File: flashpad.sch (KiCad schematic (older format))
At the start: 23 parts, among them SW1 BOOT, SW2 RESET, U1 ATmega328P-PU, U2 ATmega32A-PU

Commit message: rev2
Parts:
- removed C3, C4, C5: 100n, Capacitor_THT:C_Disc_D5.0mm_W2.5mm_P2.50mm, symbol Device:C_Small
- removed ISP1: AVR-ISP-6, Connector_PinHeader_2.54mm:PinHeader_2x03_P2.54mm_Horizontal, symbol Connector:AVR-ISP-6
- removed R5: 1.5K, Resistor_THT:R_Axial_DIN0204_L3.6mm_D1.6mm_P7.62mm_Horizontal, symbol Device:R
- removed SW1: BOOT, Button_Switch_THT:SW_PUSH_6mm, symbol Switch:SW_Push
- removed SW2: RESET, Button_Switch_THT:SW_PUSH_6mm, symbol Switch:SW_Push
- removed USB1: USB_B_Mini, custom_parts:USB_Mini, symbol Connector:USB_B_Mini
- added C1: 22p, Capacitor_THT:C_Disc_D5.0mm_W2.5mm_P5.00mm, symbol Device:C_Small
- added C8, C9: 100n, Capacitor_THT:C_Disc_D5.0mm_W2.5mm_P2.50mm, symbol Device:C_Small
- added J1: AVR-ISP-10, Connector_PinHeader_2.54mm:PinHeader_2x05_P2.54mm_Vertical, symbol Connector:AVR-ISP-10
- added JP1: SelfProg, Connector_PinHeader_2.54mm:PinHeader_1x02_P2.54mm_Vertical, symbol Device:Jumper
- added JP2: SlowSCK, Connector_PinHeader_2.54mm:PinHeader_1x02_P2.54mm_Vertical, symbol Device:Jumper
- added LED2: LED, LED_THT:LED_D5.0mm, symbol Device:LED
- added R1: 10k, Resistor_THT:R_Axial_DIN0204_L3.6mm_D1.6mm_P7.62mm_Horizontal, symbol Device:R
- added R10, R9: 1.5K, Resistor_THT:R_Axial_DIN0204_L3.6mm_D1.6mm_P7.62mm_Horizontal, symbol Device:R
- added R2, R3: 270r, Resistor_THT:R_Axial_DIN0204_L3.6mm_D1.6mm_P7.62mm_Horizontal, symbol Device:R
- added U1: ATmega8A-PU, Package_DIP:DIP-28_W7.62mm, symbol MCU_Microchip_ATmega:ATmega8A-PU
- added USB1: USB_B, Connector_USB:USB_B_OST_USB-B1HSxx_Horizontal, symbol Connector:USB_B
- added X1: 12Mhz, Crystal:Crystal_HC49-4H_Vertical, symbol Device:Crystal
- C2: value 100n -> 22p; footprint Capacitor_THT:C_Disc_D5.0mm_W2.5mm_P2.50mm -> Capacitor_THT:C_Disc_D5.0mm_W2.5mm_P5.00mm
- LED1: footprint LED_THT:LED_D3.0mm -> LED_THT:LED_D5.0mm
- R4: value 1.5K -> 270r
- R5: renamed from R1; value 1.5K -> 2.2k
- U2: footprint Package_DIP:DIP-40_W15.24mm_Socket -> Socket:DIP_Socket-40_W11.9_W12.7_W15.24_W17.78_W18.5_3M_240-1280-00-0602J
- U3: renamed from U1; footprint Package_DIP:DIP-28_W7.62mm_Socket -> custom_parts:DIP_Socket-28_flipped
- X2: renamed from XTAL1; value Crystal -> 16Mhz
- renumbered C6 to C10, C7 to C11, C1 to C3, R2 to R6, R3 to R7
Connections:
- net +5V: now also C8.1, C9.1, J1.2 (VCC), R1.1, U1.20 (AVCC), U1.7 (VCC); no longer C2.1, LED1.2 (A), R4.2
- net D+: now also U1.15 (PB1), U1.4 (PD2); no longer U2.16 (PD2), U3.4 (PD2)
- net D-: now also U1.14 (PB0); no longer U2.17 (PD3), U3.5 (PD3)
- net GND: now also C1.2, C8.2, C9.2, J1.10 (GND), J1.4 (GND), J1.6 (GND), J1.8 (GND), JP2.2, R10.1, R9.1, U1.22 (AGND), U1.8 (GND), USB1.4 (GND), USB1.5 (Shield)
- net MISO: now also U2.7 (PB6), J1.9 (MISO), U1.18 (PB4); no longer U2.6 (PB5)
- net MOSI: now also U2.6 (PB5), J1.1 (MOSI), R3.2; no longer U2.5 (PB4)
- net RESET: now also J1.5 (~RST), JP1.2, R1.2, U1.1 (PC6/~RESET); no longer R4.1
- net SCK: now also R4.2, U2.8 (PB7), J1.7 (SCK); no longer U2.7 (PB6)
- net VCC: now also USB1.1 (VBUS)
- net at D1.1 (K), R5.2, R7.1: now also USB1.2 (D-)
- net at D2.1 (K), R6.1: now also USB1.3 (D+)
- net at LED1.1 (K): now also R9.2
- net BOOT: no longer names the net of U3.6 (PD4)
- net BOOT: no longer U2.18 (PD4)
- net XTAL1 renamed XTAL2_1
- net XTAL2 renamed XTAL2_2
- new net: JP2.1, U1.25 (PC2)
- new net: JP1.1, R2.2
- new net: R2.1, U1.16 (PB2)
- new net: R3.1, U1.17 (PB3)
- new net: R4.1, U1.19 (PB5)
- new net: LED2.1 (K), R10.2
- new net LED1: LED1.2 (A), U1.23 (PC0)
- new net LED2: LED2.2 (A), U1.24 (PC1)
- new net XTAL1_1: C1.1, U1.9 (PB6/XTAL1), X1.1
- new net XTAL1_2: C2.1, U1.10 (PB7/XTAL2), X1.2
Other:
- moved on the sheet: C10, C11, C3, D1, D2, F1, R5, R6, R7, U2, U3, X2

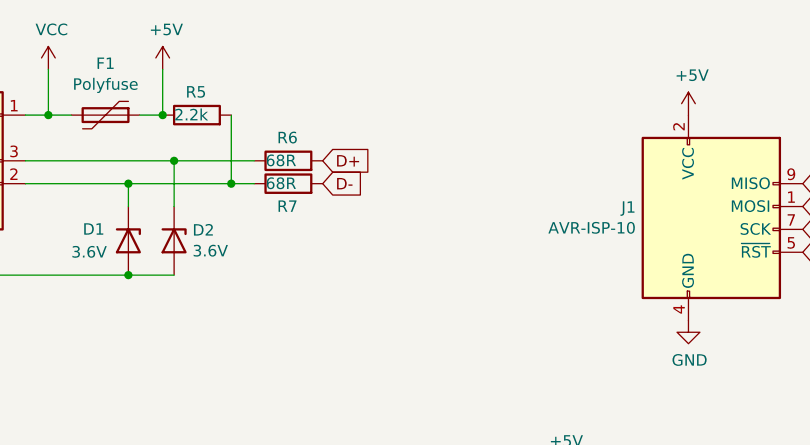
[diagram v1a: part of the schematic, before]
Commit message: fix footprints
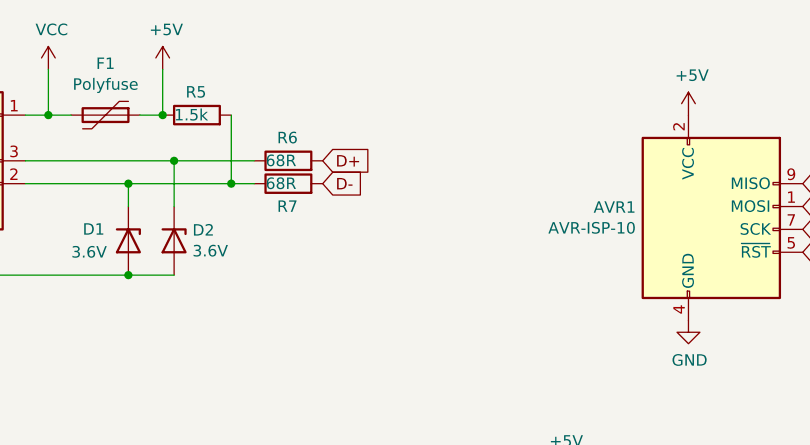
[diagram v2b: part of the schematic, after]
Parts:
- removed J1: AVR-ISP-10, Connector_PinHeader_2.54mm:PinHeader_2x05_P2.54mm_Vertical, symbol Connector:AVR-ISP-10
- added AVR1: AVR-ISP-10, Connector_IDC:IDC-Header_2x05_P2.54mm_Vertical, symbol Connector:AVR-ISP-10
- R1, R10, R2, R3, R4, R6, R7, R9: footprint Resistor_THT:R_Axial_DIN0204_L3.6mm_D1.6mm_P7.62mm_Horizontal -> Resistor_THT:R_Axial_DIN0207_L6.3mm_D2.5mm_P10.16mm_Horizontal
- R5: value 2.2k -> 1.5k; footprint Resistor_THT:R_Axial_DIN0204_L3.6mm_D1.6mm_P7.62mm_Horizontal -> Resistor_THT:R_Axial_DIN0207_L6.3mm_D2.5mm_P10.16mm_Horizontal
- U2: footprint Socket:DIP_Socket-40_W11.9_W12.7_W15.24_W17.78_W18.5_3M_240-1280-00-0602J -> custom_parts:socket40dip
- U3: footprint custom_parts:DIP_Socket-28_flipped -> custom_parts:socket28dip
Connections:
- net +5V: now also AVR1.2 (VCC)
- net GND: now also AVR1.10 (GND), AVR1.4 (GND), AVR1.6 (GND), AVR1.8 (GND)
- net MISO: now also AVR1.9 (MISO)
- net MOSI: now also AVR1.1 (MOSI)
- net RESET: now also AVR1.5 (~RST)
- net SCK: now also AVR1.7 (SCK)
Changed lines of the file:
@@
 F 0 "U3" H 7356 3746 50  0000 R CNN
 F 1 "ATmega328P-PU" H 7356 3655 50  0000 R CNN
-F 2 "custom_parts:DIP_Socket-28_flipped" H 8000 3700 50  0001 C CIN
+F 2 "custom_parts:socket28dip" H 8000 3700 50  0001 C CIN
 F 3 "http://ww1.microchip.com/downloads/en/DeviceDoc/ATmega328_P%20AVR%20MCU%20with%20picoPower%20Technology%20Data%20Sheet%2040001984A.pdf" H 8000 3700 50  0001 C CNN
 	1    8000 3700
@@
 F 0 "U2" H 10300 1650 50  0000 C CNN
 F 1 "ATmega32A-PU" H 9700 1650 50  0000 C CNN
-F 2 "Socket:DIP_Socket-40_W11.9_W12.7_W15.24_W17.78_W18.5_3M_240-1280-00-0602J" H 10150 3600 50  0001 C CIN
+F 2 "custom_parts:socket40dip" H 10150 3600 50  0001 C CIN
 F 3 "http://ww1.microchip.com/downloads/en/DeviceDoc/atmel-8155-8-bit-microcontroller-avr-atmega32a_datasheet.pdf" H 10150 3600 50  0001 C CNN
 	1    10150 3600
@@
 F 0 "R6" V 2850 1450 50  0000 R CNN
 F 1 "68R" V 2750 1500 50  0000 R CNN
-F 2 "Resistor_THT:R_Axial_DIN0204_L3.6mm_D1.6mm_P7.62mm_Horizontal" V 2680 1400 50  0001 C CNN
+F 2 "Resistor_THT:R_Axial_DIN0207_L6.3mm_D2.5mm_P10.16mm_Horizontal" V 2680 1400 50  0001 C CNN
 F 3 "~" H 2750 1400 50  0001 C CNN
 	1    2750 1400
@@
 P 2350 1200
 F 0 "R5" V 2450 1250 50  0000 R CNN
-F 1 "2.2k" V 2350 1300 50  0000 R CNN
-F 2 "Resistor_THT:R_Axial_DIN0204_L3.6mm_D1.6mm_P7.62mm_Horizontal" V 2280 1200 50  0001 C CNN
+F 1 "1.5k" V 2350 1300 50  0000 R CNN
+F 2 "Resistor_THT:R_Axial_DIN0207_L6.3mm_D2.5mm_P10.16mm_Horizontal" V 2280 1200 50  0001 C CNN
 F 3 "~" H 2350 1200 50  0001 C CNN
 	1    2350 1200
@@
 F 0 "R7" V 2650 1550 50  0000 R CNN
 F 1 "68R" V 2750 1600 50  0000 R CNN
-F 2 "Resistor_THT:R_Axial_DIN0204_L3.6mm_D1.6mm_P7.62mm_Horizontal" V 2680 1500 50  0001 C CNN
+F 2 "Resistor_THT:R_Axial_DIN0207_L6.3mm_D2.5mm_P10.16mm_Horizontal" V 2680 1500 50  0001 C CNN
 F 3 "~" H 2750 1500 50  0001 C CNN
 	1    2750 1500
@@
 F 0 "R9" V 1550 3400 50  0000 R CNN
 F 1 "1.5K" V 1450 3450 50  0000 R CNN
-F 2 "Resistor_THT:R_Axial_DIN0204_L3.6mm_D1.6mm_P7.62mm_Horizontal" V 1380 3350 50  0001 C CNN
+F 2 "Resistor_THT:R_Axial_DIN0207_L6.3mm_D2.5mm_P10.16mm_Horizontal" V 1380 3350 50  0001 C CNN
 F 3 "~" H 1450 3350 50  0001 C CNN
 	1    1450 3350
@@
 F 0 "R1" V 3050 3200 50  0000 R CNN
 F 1 "10k" V 2950 3250 50  0000 R CNN
-F 2 "Resistor_THT:R_Axial_DIN0204_L3.6mm_D1.6mm_P7.62mm_Horizontal" V 2880 3150 50  0001 C CNN
+F 2 "Resistor_THT:R_Axial_DIN0207_L6.3mm_D2.5mm_P10.16mm_Horizontal" V 2880 3150 50  0001 C CNN
 F 3 "~" H 2950 3150 50  0001 C CNN
 	1    2950 3150
@@
 F 0 "R2" V 5100 3400 50  0000 R CNN
 F 1 "270r" V 5000 3450 50  0000 R CNN
-F 2 "Resistor_THT:R_Axial_DIN0204_L3.6mm_D1.6mm_P7.62mm_Horizontal" V 4930 3350 50  0001 C CNN
+F 2 "Resistor_THT:R_Axial_DIN0207_L6.3mm_D2.5mm_P10.16mm_Horizontal" V 4930 3350 50  0001 C CNN
 F 3 "~" H 5000 3350 50  0001 C CNN
 	1    5000 3350
@@
 F 0 "R3" V 4900 3500 50  0000 R CNN
 F 1 "270r" V 4800 3550 50  0000 R CNN
-F 2 "Resistor_THT:R_Axial_DIN0204_L3.6mm_D1.6mm_P7.62mm_Horizontal" V 4730 3450 50  0001 C CNN
+F 2 "Resistor_THT:R_Axial_DIN0207_L6.3mm_D2.5mm_P10.16mm_Horizontal" V 4730 3450 50  0001 C CNN
 F 3 "~" H 4800 3450 50  0001 C CNN
 	1    4800 3450
@@
 F 0 "R4" V 5100 3700 50  0000 R CNN
 F 1 "270r" V 5000 3750 50  0000 R CNN
-F 2 "Resistor_THT:R_Axial_DIN0204_L3.6mm_D1.6mm_P7.62mm_Horizontal" V 4930 3650 50  0001 C CNN
+F 2 "Resistor_THT:R_Axial_DIN0207_L6.3mm_D2.5mm_P10.16mm_Horizontal" V 4930 3650 50  0001 C CNN
 F 3 "~" H 5000 3650 50  0001 C CNN
 	1    5000 3650
@@
 F 0 "R10" V 1550 4000 50  0000 R CNN
 F 1 "1.5K" V 1450 4050 50  0000 R CNN
-F 2 "Resistor_THT:R_Axial_DIN0204_L3.6mm_D1.6mm_P7.62mm_Horizontal" V 1380 3950 50  0001 C CNN
+F 2 "Resistor_THT:R_Axial_DIN0207_L6.3mm_D2.5mm_P10.16mm_Horizontal" V 1380 3950 50  0001 C CNN
 F 3 "~" H 1450 3950 50  0001 C CNN
 	1    1450 3950
@@
 Wire Wire Line
 	1300 3950 1150 3950
-$Comp
-L Connector:AVR-ISP-10 J1
-U 1 1 60B58B23
-P 4600 1700
-F 0 "J1" H 4270 1796 50  0000 R CNN
-F 1 "AVR-ISP-10" H 4270 1705 50  0000 R CNN
-F 2 "Connector_PinHeader_2.54mm:PinHeader_2x05_P2.54mm_Vertical" V 4350 1750 50  0001 C CNN
-F 3 " ~" H 3325 1150 50  0001 C CNN
-	1    4600 1700
-	1    0    0    -1
-$EndComp
 Text GLabel 5000 1600 2    50   Input ~ 0
 MOSI
@@
 $EndComp
 Connection ~ 1300 1800
+$Comp
+L Connector:AVR-ISP-10 AVR1
+U 1 1 60AD06FA
+P 4600 1700
+F 0 "AVR1" H 4270 1796 50  0000 R CNN
+F 1 "AVR-ISP-10" H 4270 1705 50  0000 R CNN
+F 2 "Connector_IDC:IDC-Header_2x05_P2.54mm_Vertical" V 4350 1750 50  0001 C CNN
+F 3 " ~" H 3325 1150 50  0001 C CNN
+	1    4600 1700
+	1    0    0    -1
+$EndComp
 $EndSCHEMATC

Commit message: fix prototype issues
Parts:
- removed R2, R3, R4: 270r, Resistor_THT:R_Axial_DIN0207_L6.3mm_D2.5mm_P10.16mm_Horizontal, symbol Device:R
- added R5: 10k, Resistor_THT:R_Axial_DIN0207_L6.3mm_D2.5mm_P10.16mm_Horizontal, symbol Device:R
- renumbered C3 to C1, C8 to C2, C9 to C3, C1 to C4, C2 to C5, C10 to C6, C11 to C7, R5 to R2, R6 to R3, R7 to R4, R9 to R6, R10 to R7
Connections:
- net +5V: now also R5.2
- net MOSI: now also U1.17 (PB3)
- net RESET: now also U1.16 (PB2), R5.1; no longer R1.2, U1.1 (PC6/~RESET)
- net SCK: now also U1.19 (PB5)
- net at JP1.1: now also R1.2, U1.1 (PC6/~RESET)
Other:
- moved on the sheet: JP1
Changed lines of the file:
@@
 $EndComp
 $Comp
-L Device:C_Small C10
+L Device:C_Small C6
 U 1 1 5EE9A052
 P 1350 5300
-F 0 "C10" H 1150 5350 50  0000 L CNN
+F 0 "C6" H 1150 5350 50  0000 L CNN
 F 1 "22p" H 1100 5250 50  0000 L CNN
 F 2 "Capacitor_THT:C_Disc_D5.0mm_W2.5mm_P5.00mm" H 1350 5300 50  0001 C CNN
@@
 $EndComp
 $Comp
-L Device:C_Small C11
+L Device:C_Small C7
 U 1 1 5EE9A831
 P 1650 5300
-F 0 "C11" H 1742 5346 50  0000 L CNN
+F 0 "C7" H 1742 5346 50  0000 L CNN
 F 1 "22p" H 1742 5255 50  0000 L CNN
 F 2 "Capacitor_THT:C_Disc_D5.0mm_W2.5mm_P5.00mm" H 1650 5300 50  0001 C CNN
@@
 $EndComp
 $Comp
-L Device:CP1_Small C3
+L Device:CP1_Small C1
 U 1 1 5EE9B7B5
 P 3000 7150
-F 0 "C3" H 2800 7200 50  0000 L CNN
+F 0 "C1" H 2800 7200 50  0000 L CNN
 F 1 "4.7u" H 2750 7100 50  0000 L CNN
 F 2 "Capacitor_THT:CP_Radial_D4.0mm_P2.00mm" H 3000 7150 50  0001 C CNN
@@
 D-
 $Comp
-L Device:R R6
+L Device:R R3
 U 1 1 5EEC1ED5
 P 2750 1400
-F 0 "R6" V 2850 1450 50  0000 R CNN
+F 0 "R3" V 2850 1450 50  0000 R CNN
 F 1 "68R" V 2750 1500 50  0000 R CNN
 F 2 "Resistor_THT:R_Axial_DIN0207_L6.3mm_D2.5mm_P10.16mm_Horizontal" V 2680 1400 50  0001 C CNN
@@
 $EndComp
 $Comp
-L Device:R R5
+L Device:R R2
 U 1 1 5EEC3D5B
 P 2350 1200
-F 0 "R5" V 2450 1250 50  0000 R CNN
+F 0 "R2" V 2450 1250 50  0000 R CNN
 F 1 "1.5k" V 2350 1300 50  0000 R CNN
 F 2 "Resistor_THT:R_Axial_DIN0207_L6.3mm_D2.5mm_P10.16mm_Horizontal" V 2280 1200 50  0001 C CNN
@@
 	1600 1400 2250 1400
 $Comp
-L Device:R R7
+L Device:R R4
 U 1 1 5EECA7F9
 P 2750 1500
-F 0 "R7" V 2650 1550 50  0000 R CNN
+F 0 "R4" V 2650 1550 50  0000 R CNN
 F 1 "68R" V 2750 1600 50  0000 R CNN
 F 2 "Resistor_THT:R_Axial_DIN0207_L6.3mm_D2.5mm_P10.16mm_Horizontal" V 2680 1500 50  0001 C CNN
@@
 $EndComp
 $Comp
-L Device:R R9
+L Device:R R6
 U 1 1 609373FA
 P 1450 3350
-F 0 "R9" V 1550 3400 50  0000 R CNN
+F 0 "R6" V 1550 3400 50  0000 R CNN
 F 1 "1.5K" V 1450 3450 50  0000 R CNN
 F 2 "Resistor_THT:R_Axial_DIN0207_L6.3mm_D2.5mm_P10.16mm_Horizontal" V 1380 3350 50  0001 C CNN
@@
 $EndComp
 $Comp
-L Device:C_Small C1
+L Device:C_Small C4
 U 1 1 6093F86D
 P 1350 6600
-F 0 "C1" H 1150 6650 50  0000 L CNN
+F 0 "C4" H 1150 6650 50  0000 L CNN
 F 1 "22p" H 1100 6550 50  0000 L CNN
 F 2 "Capacitor_THT:C_Disc_D5.0mm_W2.5mm_P5.00mm" H 1350 6600 50  0001 C CNN
@@
 $EndComp
 $Comp
-L Device:C_Small C2
+L Device:C_Small C5
 U 1 1 6093F877
 P 1650 6600
-F 0 "C2" H 1742 6646 50  0000 L CNN
+F 0 "C5" H 1742 6646 50  0000 L CNN
 F 1 "22p" H 1742 6555 50  0000 L CNN
 F 2 "Capacitor_THT:C_Disc_D5.0mm_W2.5mm_P5.00mm" H 1650 6600 50  0001 C CNN
@@
 D+
 $Comp
-L Device:C_Small C8
+L Device:C_Small C2
 U 1 1 6094C747
 P 3450 7150
-F 0 "C8" H 3542 7196 50  0000 L CNN
+F 0 "C2" H 3542 7196 50  0000 L CNN
 F 1 "100n" H 3542 7105 50  0000 L CNN
 F 2 "Capacitor_THT:C_Disc_D5.0mm_W2.5mm_P2.50mm" H 3450 7150 50  0001 C CNN
@@
 $EndComp
 $Comp
-L Device:C_Small C9
+L Device:C_Small C3
 U 1 1 6094F111
 P 3800 7150
-F 0 "C9" H 3892 7196 50  0000 L CNN
+F 0 "C3" H 3892 7196 50  0000 L CNN
 F 1 "100n" H 3892 7105 50  0000 L CNN
 F 2 "Capacitor_THT:C_Disc_D5.0mm_W2.5mm_P2.50mm" H 3800 7150 50  0001 C CNN
@@
 L Device:Jumper JP1
 U 1 1 6094F55F
-P 5450 3350
-F 0 "JP1" H 5450 3614 50  0000 C CNN
-F 1 "SelfProg" H 5450 3523 50  0000 C CNN
-F 2 "Connector_PinHeader_2.54mm:PinHeader_1x02_P2.54mm_Vertical" H 5450 3350 50  0001 C CNN
-F 3 "~" H 5450 3350 50  0001 C CNN
-	1    5450 3350
-	1    0    0    -1
-$EndComp
-Wire Wire Line
-	4550 3350 4850 3350
-Text GLabel 3200 3000 1    50   Input ~ 0
+P 3200 2700
+F 0 "JP1" H 3200 2964 50  0000 C CNN
+F 1 "SelfProg" H 3200 2873 50  0000 C CNN
+F 2 "Connector_PinHeader_2.54mm:PinHeader_1x02_P2.54mm_Vertical" H 3200 2700 50  0001 C CNN
+F 3 "~" H 3200 2700 50  0001 C CNN
+	1    3200 2700
+	0    -1   -1   0
+$EndComp
+Text GLabel 3200 2400 1    50   Input ~ 0
 RESET
-Text GLabel 5750 3350 2    50   Input ~ 0
+Text GLabel 5000 3350 2    50   Input ~ 0
 RESET
 $Comp
@@
 Wire Wire Line
 	2650 3150 2800 3150
-Text GLabel 5750 3450 2    50   Input ~ 0
+Text GLabel 5050 3450 2    50   Input ~ 0
 MOSI
-$Comp
-L Device:R R2
-U 1 1 60969135
-P 5000 3350
-F 0 "R2" V 5100 3400 50  0000 R CNN
-F 1 "270r" V 5000 3450 50  0000 R CNN
-F 2 "Resistor_THT:R_Axial_DIN0207_L6.3mm_D2.5mm_P10.16mm_Horizontal" V 4930 3350 50  0001 C CNN
-F 3 "~" H 5000 3350 50  0001 C CNN
-	1    5000 3350
-	0    -1   -1   0
-$EndComp
-$Comp
-L Device:R R3
-U 1 1 60969BB0
-P 4800 3450
-F 0 "R3" V 4900 3500 50  0000 R CNN
-F 1 "270r" V 4800 3550 50  0000 R CNN
-F 2 "Resistor_THT:R_Axial_DIN0207_L6.3mm_D2.5mm_P10.16mm_Horizontal" V 4730 3450 50  0001 C CNN
-F 3 "~" H 4800 3450 50  0001 C CNN
-	1    4800 3450
-	0    -1   -1   0
-$EndComp
-Wire Wire Line
-	4550 3450 4650 3450
-Wire Wire Line
-	4950 3450 5750 3450
-$Comp
-L Device:R R4
-U 1 1 6097035F
-P 5000 3650
-F 0 "R4" V 5100 3700 50  0000 R CNN
-F 1 "270r" V 5000 3750 50  0000 R CNN
-F 2 "Resistor_THT:R_Axial_DIN0207_L6.3mm_D2.5mm_P10.16mm_Horizontal" V 4930 3650 50  0001 C CNN
-F 3 "~" H 5000 3650 50  0001 C CNN
-	1    5000 3650
-	0    -1   -1   0
-$EndComp
-Text GLabel 5750 3550 2    50   Input ~ 0
+Text GLabel 5050 3550 2    50   Input ~ 0
 MISO
-Wire Wire Line
-	4550 3650 4850 3650
-Wire Wire Line
-	4550 3550 5750 3550
-Wire Wire Line
-	5150 3650 5750 3650
-Text GLabel 5750 3650 2    50   Input ~ 0
+Text GLabel 5050 3650 2    50   Input ~ 0
 SCK
 Text GLabel 8600 3200 2    50   Input ~ 0
@@
 $EndComp
 $Comp
-L Device:R R10
+L Device:R R7
 U 1 1 60B1D103
 P 1450 3950
-F 0 "R10" V 1550 4000 50  0000 R CNN
+F 0 "R7" V 1550 4000 50  0000 R CNN
 F 1 "1.5K" V 1450 4050 50  0000 R CNN
 F 2 "Resistor_THT:R_Axial_DIN0207_L6.3mm_D2.5mm_P10.16mm_Horizontal" V 1380 3950 50  0001 C CNN
@@
 	1    0    0    -1
 $EndComp
+Wire Wire Line
+	4550 3350 5000 3350
+Wire Wire Line
+	4550 3450 5050 3450
+Wire Wire Line
+	4550 3550 5050 3550
+Wire Wire Line
+	4550 3650 5050 3650
+$Comp
+L Device:R R5
+U 1 1 60B3D36B
+P 5500 2550
+F 0 "R5" V 5600 2600 50  0000 R CNN
+F 1 "10k" V 5500 2650 50  0000 R CNN
+F 2 "Resistor_THT:R_Axial_DIN0207_L6.3mm_D2.5mm_P10.16mm_Horizontal" V 5430 2550 50  0001 C CNN
+F 3 "~" H 5500 2550 50  0001 C CNN
+	1    5500 2550
+	0    1    1    0
+$EndComp
+$Comp
+L power:+5V #PWR0104
+U 1 1 60B3DBF3
+P 5150 2550
+F 0 "#PWR0104" H 5150 2400 50  0001 C CNN
+F 1 "+5V" H 5165 2723 50  0000 C CNN
+F 2 "" H 5150 2550 50  0001 C CNN
+F 3 "" H 5150 2550 50  0001 C CNN
+	1    5150 2550
+	1    0    0    -1
+$EndComp
+Wire Wire Line
+	5350 2550 5150 2550
+Wire Wire Line
+	5800 2550 5650 2550
+Text GLabel 5800 2550 2    50   Input ~ 0
+RESET
 $EndSCHEMATC
